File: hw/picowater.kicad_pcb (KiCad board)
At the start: 2 copper layers, 98 x 56 mm, 47 parts, among them J1 +12V, J10 Batt TP, J13 RJ45, J14 RJ45, J15 RJ45, J2 Power In, J4 UART, J6 JST-PH2 Bat, J7 GPIO2, J9 5V TP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

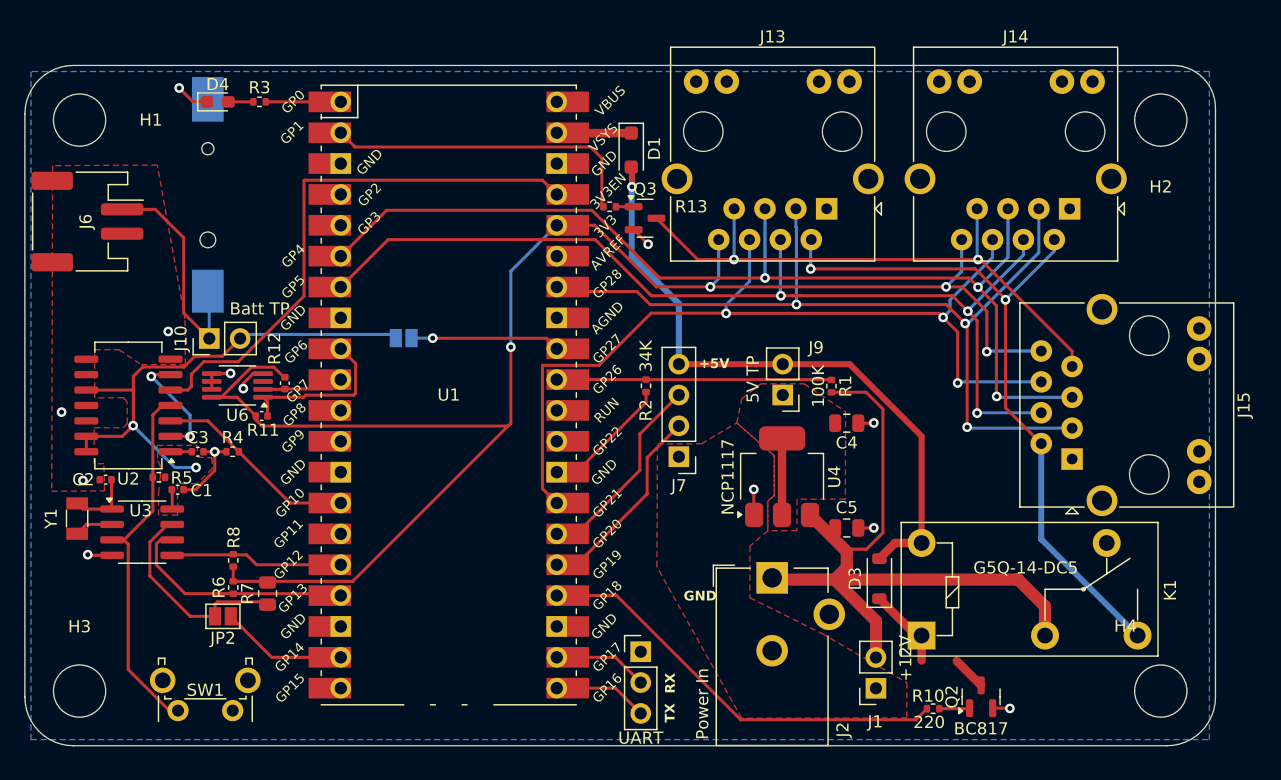
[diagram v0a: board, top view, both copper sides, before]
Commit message: fw: send info to server, pcb: many tweaks
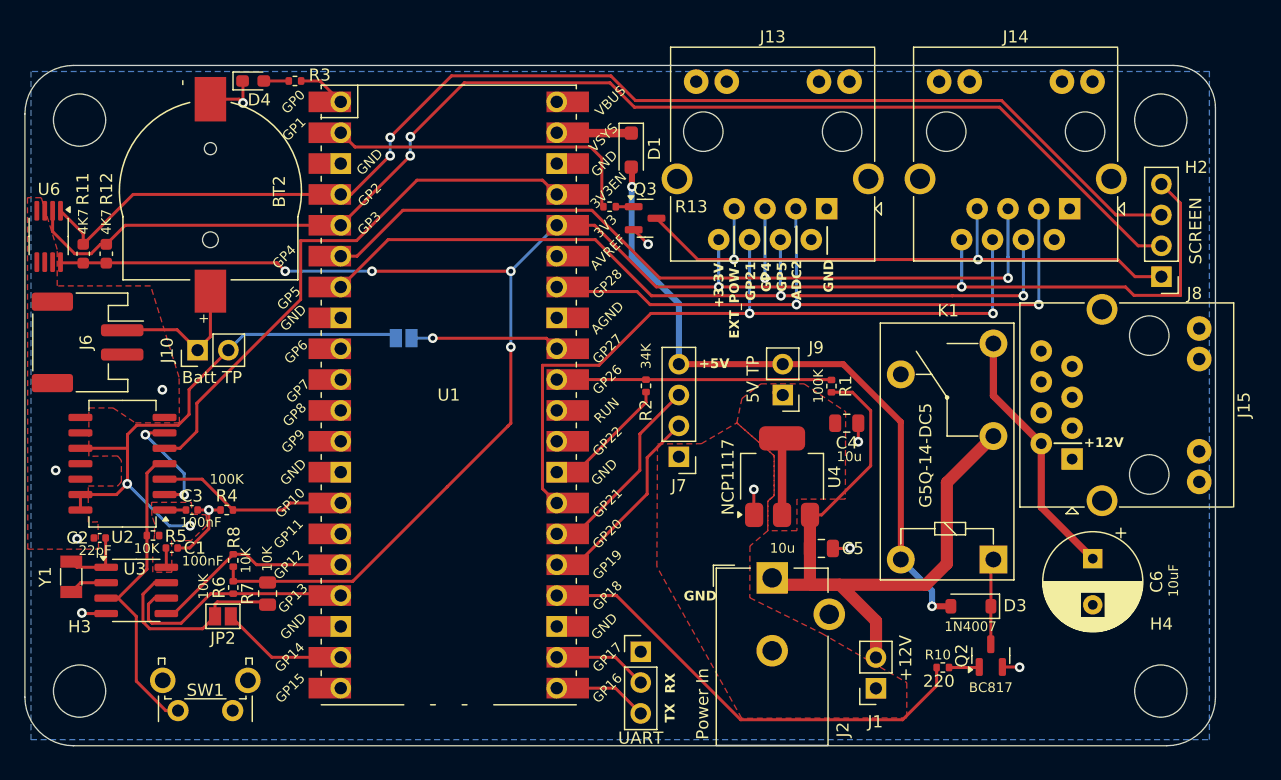
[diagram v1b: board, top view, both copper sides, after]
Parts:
- added C6: 10uF, Capacitor_THT:CP_Radial_D8.0mm_P3.80mm, F.Cu at (141.9, 108.6)
- added J8: SCREEN, Connector_PinHeader_2.54mm:PinHeader_1x04_P2.54mm_Vertical, F.Cu at (147.6, 85.4)
- BT2: moved to F.Cu
- R11, R12: footprint Capacitor_SMD:C_0402_1005Metric -> Capacitor_SMD:C_0603_1608Metric
- moved R11 19.9 mm to (58.8, 83.5), turned to 90 degrees
- moved U6 19.8 mm to (56.0, 82.1), turned to -90 degrees
- moved R12 18.2 mm to (60.7, 83.5), turned to 90 degrees
- moved J6 9.95 mm to (59.2, 90.8)
- moved K1 8.61 mm to (133.7, 108.7), turned to 90 degrees
- moved D3 7.86 mm to (131.9, 112.5), turned to 180 degrees
- moved C1 4.82 mm to (66.1, 107.7)
- moved C2 4.82 mm to (60.2, 106.9)
- moved C3 4.82 mm to (67.7, 104.6)
- moved R4 4.82 mm to (70.6, 104.6)
- moved U2 4.82 mm to (62.0, 100.8)
- moved Y1 4.82 mm to (57.8, 110.1)
- moved R5 4.82 mm to (64.5, 106.7)
- moved U3 4.82 mm to (63.2, 111.2)
- moved R10 3.48 mm to (129.6, 117.6)
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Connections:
- J13 pad 2: PUMP+12V -> unconnected-(J13-Pad2)
- J14 pad 2: PUMP+12V -> unconnected-(J14-Pad2)
- J15 pad 3: ADC2 -> unconnected-(J15-Pad3)
- J15 pad 4: GPIO5 -> unconnected-(J15-Pad4)
- J15 pad 5: GPIO4 -> unconnected-(J15-Pad5)
- J15 pad 6: GPIO21 -> unconnected-(J15-Pad6)
- J15 pad 7: EXT_POWER- -> unconnected-(J15-Pad7)
- J15 pad 8: +3.3V -> unconnected-(J15-Pad8)
- U1 pad 10: I2C1-SCL -> unconnected-(U1-GPIO7-Pad10)_1
- U1 pad 4: GPIO2 -> I2C1-SDA
- U1 pad 5: GPIO3 -> I2C1-SCL
- U1 pad 9: I2C1-SDA -> unconnected-(U1-GPIO6-Pad9)_1
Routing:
- net I2C1-SCL: track 6.73 -> 106.0 mm, vias 0 -> 2
- net I2C1-SDA: track 13.6 -> 103.7 mm, vias 0 -> 2
- net PUMP+12V: track 58.2 -> 21.1 mm, vias 2 -> 0
- net +3.3V: track 135.1 -> 156.1 mm, vias 4 -> 6
- net ADC2: track 72.1 -> 56.1 mm, vias 3 -> 2
- net GPIO4: track 85.7 -> 70.2 mm, vias 3 -> 2
- net GPIO5: track 82.1 -> 69.0 mm, vias 3 -> 2
- net GPIO21: track 74.5 -> 62.9 mm, vias 3 -> 2
- net RAW_BAT+: track 18.5 -> 12.2 mm
- net 1~{PRE}: track 30.3 -> 25.9 mm
- net +BATT: track 46.6 -> 50.3 mm
- net EXT_POWER-: track 48.4 -> 51.9 mm
- net GPIO18: track 35.1 -> 38.2 mm
- net GND: track 35.1 -> 32.1 mm, vias 13 -> 11
- net +5V: track 53.2 -> 56.0 mm, vias 1 -> 2
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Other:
- board text added: "+12V"
- board text added: "+3.3V"
- board text added: "ADC2"
- board text added: "EXT_POW-"
- board text added: "GP21"
- board text added: "GP4"
- board text added: "GP5"

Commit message: [pcb] update
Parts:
- removed U4: NCP1117, Package_TO_SOT_SMD:SOT-223-3_TabPin2
- added C7: 1u, Capacitor_SMD:C_0603_1608Metric, F.Cu at (117.3, 96.2)
- added C8: 0.1u, Capacitor_SMD:C_0603_1608Metric, F.Cu at (113.8, 101.8)
- added C9: 0.1u, Capacitor_SMD:C_0603_1608Metric, F.Cu at (117.0, 102.0)
- added J3: 12V TP, Connector_PinHeader_2.54mm:PinHeader_1x02_P2.54mm_Vertical, F.Cu at (116.8, 107.3)
- added L1: 10uH, Capacitor_SMD:C_0805_2012Metric, F.Cu at (118.2, 98.9)
- added U5: MAX77596, Lunasys_Library:TDFN-10-EP_2.5mm, F.Cu at (115.8, 98.6)
- C4: value 10u -> 22u
- H1, H2, H3, H4: footprint MountingHole:MountingHole_4.3mm_M4 -> Lunasys_Library:hole_5mm
- moved C4 7.71 mm to (114.1, 95.9), turned to 180 degrees
- moved C5 6.99 mm to (113.2, 104.8), turned to 180 degrees
- moved R1 2.63 mm to (118.9, 92.2)
- moved J9 2.08 mm to (116.4, 93.1)
- moved J7 2.07 mm to (107.8, 98.1)
- moved J2 0.82 mm to (115.5, 111.0)
- moved J14 0.50 mm to (139.5, 79.8)
- moved R2 0.47 mm to (104.7, 94.4)
- moved K1 0.27 mm to (133.4, 108.7)
- moved J8 0.26 mm to (147.5, 85.7)
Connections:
- net Net-(U2-1D) renamed N_3V3_EN
- C5 pad 1: +12V -> Net-(J3-Pin_2)
- J13 pad 2: unconnected-(J13-Pad2) -> +5V
- J14 pad 2: unconnected-(J14-Pad2) -> +5V
- R1 pad 2: +12V -> Net-(J3-Pin_2)
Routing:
- net +5V: track 56.0 -> 90.3 mm, vias 2 -> 5
- net 3V3_EN: track 46.1 -> 72.1 mm, vias 0 -> 1
- net Net-(J3-Pin_2): track 0.00 -> 24.2 mm
- net +12V: track 57.7 -> 38.1 mm
- net GND: track 32.1 -> 18.0 mm, vias 11 -> 14
- net Net-(U5-LX): track 0.00 -> 6.99 mm, vias 0 -> 2
- net Net-(J9-Pin_1): track 6.31 -> 8.97 mm
- net Net-(J7-Pin_2): track 16.5 -> 18.6 mm
- net Net-(J7-Pin_3): track 16.5 -> 18.6 mm
- net Net-(U5-BIAS): track 0.00 -> 1.75 mm
- net Net-(U5-BST): track 0.00 -> 1.72 mm
- net GPIO5: track 69.0 -> 67.9 mm
- net GPIO21: track 62.9 -> 61.8 mm
- net GPIO4: track 70.2 -> 69.2 mm
- net ADC2: track 56.1 -> 55.1 mm
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- removed copper zone on F.Cu, net Net-(J9-Pin_1)

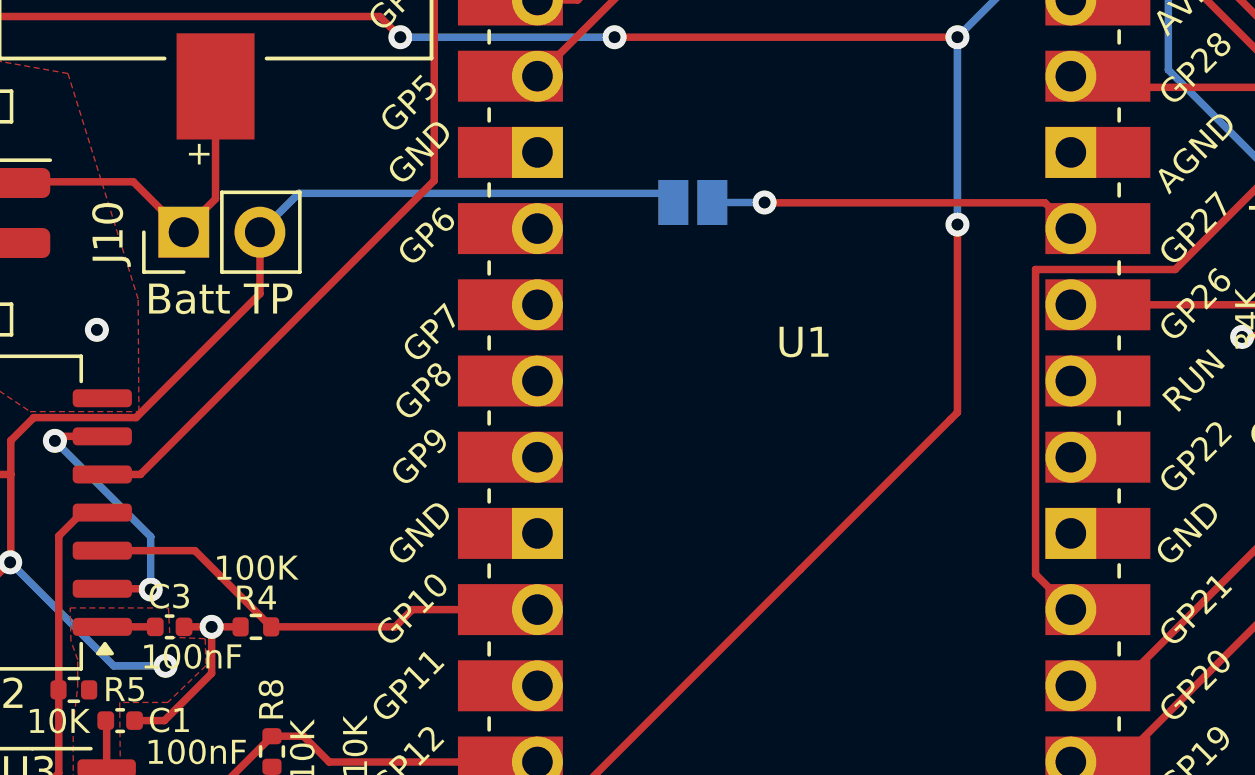
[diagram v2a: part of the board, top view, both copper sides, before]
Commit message: [pcb] fix ADC + add internal connector for int. bat
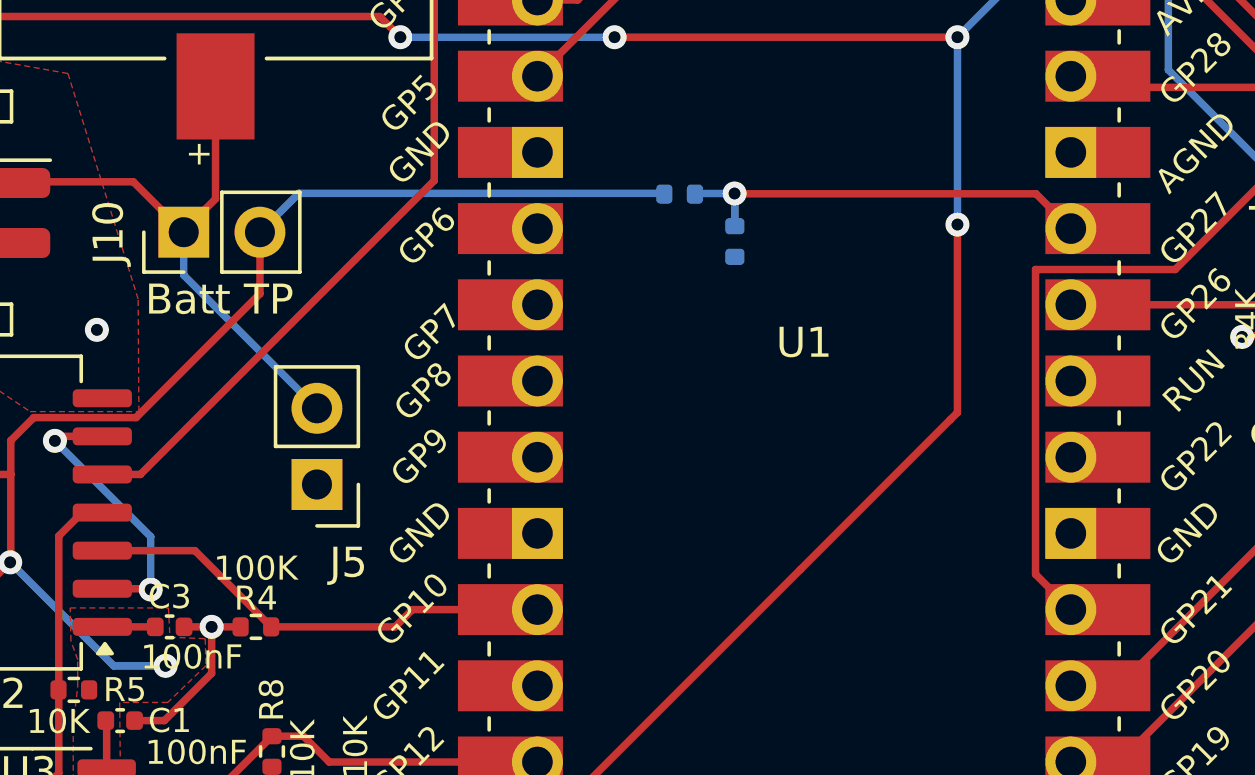
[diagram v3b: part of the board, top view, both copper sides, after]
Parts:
- removed JP3: JP_ADC_BAT, Jumper:SolderJumper-2_P1.3mm_Open_Pad1.0x1.5mm
- added J5: Int. Bat, Connector_PinHeader_2.54mm:PinHeader_1x02_P2.54mm_Vertical, F.Cu at (72.7, 99.8)
- added R14: 200K, Resistor_SMD:R_0402_1005Metric, B.Cu at (86.6, 91.8)
- added R9: 900K, Resistor_SMD:R_0402_1005Metric, B.Cu at (84.7, 90.2)
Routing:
- net RAW_BAT+: track 12.2 -> 19.9 mm
- net ADC1: track 12.3 -> 14.1 mm

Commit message: [pcb] fix diode polarity on relay
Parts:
- R14: value 200K -> 900K
- R9: value 900K -> 200K
- turned D3 to 0 degrees
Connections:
- D3 pad 1: Net-(D3-K) -> +5V
- D3 pad 2: +5V -> Net-(D3-A)
- K1 pad 1: Net-(D3-K) -> Net-(D3-A)
- Q2 pad 3: Net-(D3-K) -> Net-(D3-A)
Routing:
- net Net-(D3-K): track 7.00 -> 0.00 mm
- net Net-(D3-A): track 0.00 -> 7.00 mm
